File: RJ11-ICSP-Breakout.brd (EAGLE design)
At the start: 30.5 x 23 mm, 3 parts, among them J5 ICSP

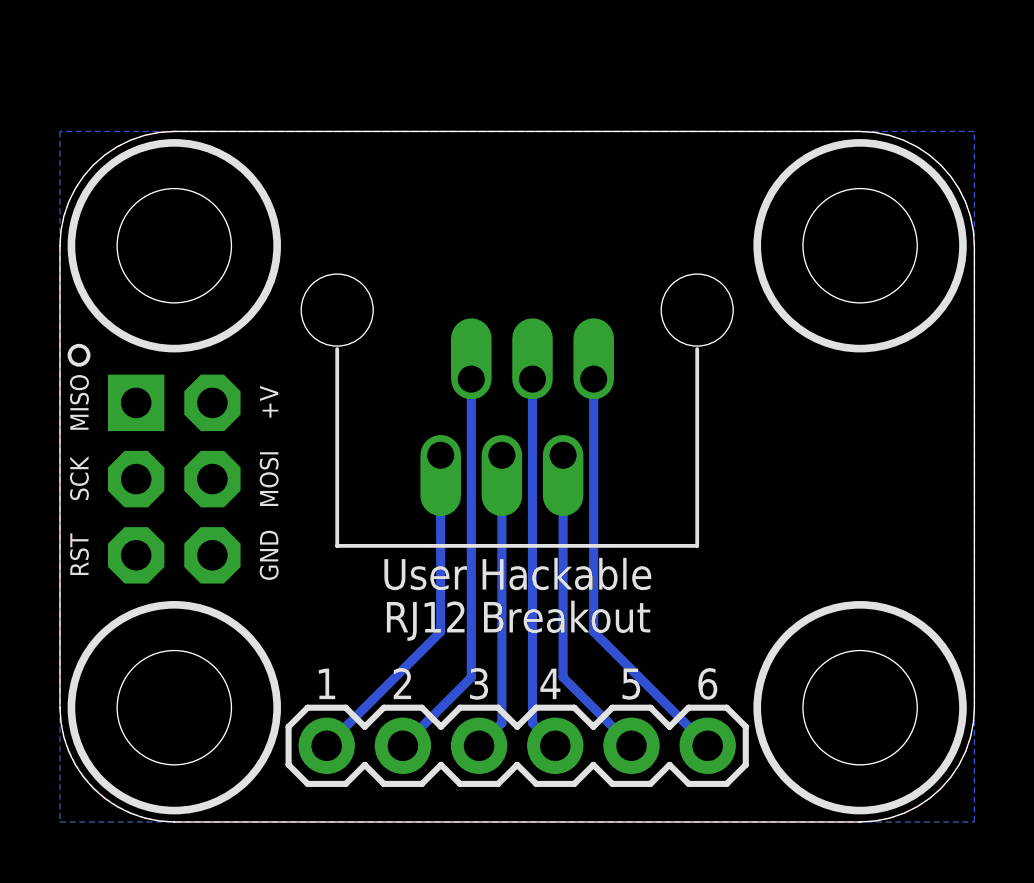
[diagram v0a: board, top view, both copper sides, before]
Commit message: updating ICSP breakout
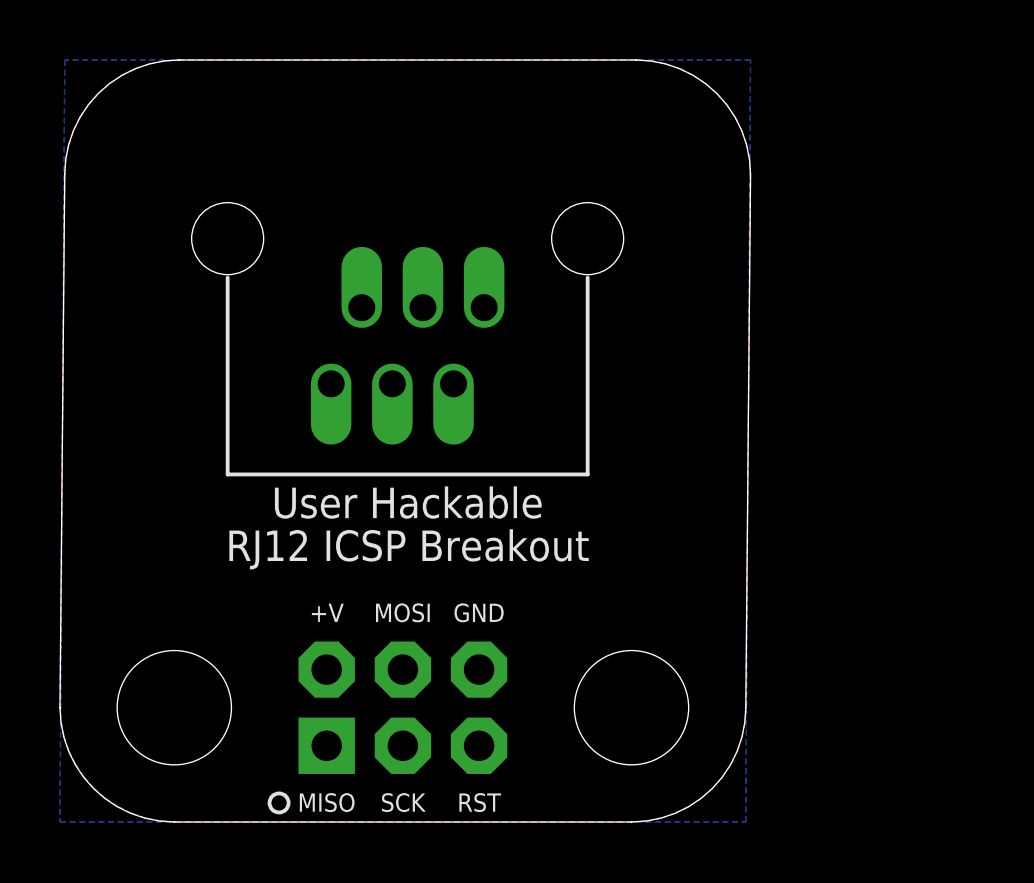
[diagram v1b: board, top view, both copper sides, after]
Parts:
- removed JP1: (no value), SparkFun-Connectors:1X06
- moved J5 10.8 mm to (11.4, 3.81), turned to 0 degrees
- moved U$7 4.36 mm to (11.6, 17.1)
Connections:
- net 4: no longer JP1.4
- net 5: no longer JP1.5
- net 5V: no longer JP1.3
- net 6: no longer JP1.6
- net GND: no longer JP1.2
- net RST: no longer JP1.1
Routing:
- net 6: track 13.8 -> 0.00 mm
- net GND: track 13.2 -> 0.00 mm
- net 4: track 12.5 -> 0.00 mm
- net RST: track 11.3 -> 0.00 mm
- net 5: track 10.6 -> 0.00 mm
- net 5V: track 10.00 -> 0.00 mm
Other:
- board size 30.5 x 23 mm -> 23 x 25.4 mm
- board text added: "RJ12 ICSP Breakout"
- board text removed: "1"
- board text removed: "2"
- board text removed: "3"
- board text removed: "4"
- board text removed: "5"
- board text removed: "6"
- board text removed: "RJ12 Breakout"
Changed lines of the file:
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@@
 <board>
 <plain>
-<wire x1="3.81" y1="0" x2="26.67" y2="0" width="0" layer="20"/>
-<wire x1="26.67" y1="0" x2="30.48" y2="3.81" width="0" layer="20" curve="90"/>
-<wire x1="30.48" y1="3.81" x2="30.48" y2="19.19554375" width="0" layer="20"/>
-<wire x1="30.48" y1="19.19554375" x2="26.65679375" y2="23.01875" width="0" layer="20" curve="90"/>
-<wire x1="26.65679375" y1="23.01875" x2="3.81" y2="23.01875" width="0" layer="20"/>
-<wire x1="3.81" y1="23.01875" x2="0" y2="19.20875" width="0" layer="20" curve="90"/>
-<wire x1="0" y1="19.20875" x2="0" y2="3.81" width="0" layer="20"/>
+<wire x1="3.81" y1="0" x2="19.05" y2="0" width="0" layer="20"/>
+<wire x1="19.05" y1="0" x2="22.86" y2="3.81" width="0" layer="20" curve="90"/>
+<wire x1="22.86" y1="3.81" x2="23.01875" y2="21.57679375" width="0" layer="20"/>
+<wire x1="23.01875" y1="21.57679375" x2="19.19554375" y2="25.4" width="0" layer="20" curve="90"/>
+<wire x1="19.19554375" y1="25.4" x2="3.96875" y2="25.4" width="0" layer="20"/>
+<wire x1="3.96875" y1="25.4" x2="0.15875" y2="21.59" width="0" layer="20" curve="90"/>
+<wire x1="0.15875" y1="21.59" x2="0" y2="3.81" width="0" layer="20"/>
 <wire x1="0" y1="3.81" x2="3.81" y2="0" width="0" layer="20" curve="90"/>
-<hole x="3.81" y="19.20875" drill="3.81"/>
 <hole x="3.81" y="3.81" drill="3.81"/>
-<circle x="3.81" y="3.81" radius="3.429" width="0.254" layer="21"/>
-<circle x="3.81" y="19.20875" radius="3.429" width="0.254" layer="21"/>
-<hole x="26.67" y="19.20875" drill="3.81"/>
-<circle x="26.67" y="19.20875" radius="3.429" width="0.254" layer="21"/>
-<hole x="26.67" y="3.81" drill="3.81"/>
-<circle x="26.67" y="3.81" radius="3.429" width="0.254" layer="21"/>
-<text x="15.24" y="8.255" size="1.016" layer="21" rot="R180" align="center">User Hackable</text>
-<text x="15.24" y="6.82625" size="1.016" layer="21" align="center">RJ12 Breakout</text>
-<text x="8.89" y="4.60375" size="1.016" layer="21" align="center">1</text>
-<text x="11.43" y="4.60375" size="1.016" layer="21" align="center">2</text>
-<text x="13.97" y="4.60375" size="1.016" layer="21" align="center">3</text>
-<text x="16.35125" y="4.60375" size="1.016" layer="21" align="center">4</text>
-<text x="19.05" y="4.60375" size="1.016" layer="21" align="center">5</text>
-<text x="21.59" y="4.60375" size="1.016" layer="21" align="center">6</text>
+<hole x="19.05" y="3.81" drill="3.81"/>
+<text x="11.58875" y="10.63625" size="1.016" layer="21" rot="R180" align="center">User Hackable</text>
+<text x="11.58875" y="9.2075" size="1.016" layer="21" align="center">RJ12 ICSP Breakout</text>
 </plain>
 <attributes>
@@
 </autorouter>
 <elements>
-<element name="J5" library="barbary_enterprises" package="2X3-NS" value="ICSP" x="3.81" y="11.43" rot="R270"/>
-<element name="U$7" library="barbary_enterprises" package="RJ12" value="RJ12" x="15.24" y="14.76375" rot="R180"/>
-<element name="JP1" library="SparkFun-Connectors" package="1X06" value="" x="8.89" y="2.54" smashed="yes">
-<attribute name="PROD_ID" value="CONN-08437" x="8.89" y="2.54" size="0.8128" layer="27" display="off"/>
-<attribute name="VALUE" x="7.62" y="-0.635" size="1.27" layer="27"/>
-</element>
+<element name="J5" library="barbary_enterprises" package="2X3-NS" value="ICSP" x="11.43" y="3.81"/>
+<element name="U$7" library="barbary_enterprises" package="RJ12" value="RJ12" x="11.58875" y="17.145" rot="R180"/>
 </elements>
 <signals>
@@
 <contactref element="J5" pad="6"/>
 <polygon width="0.4064" layer="1" isolate="0.3048">
-<vertex x="26.65679375" y="23.01875"/>
-<vertex x="3.82320625" y="23.01875" curve="90"/>
-<vertex x="0" y="19.19554375"/>
+<vertex x="19.19554375" y="25.4"/>
+<vertex x="3.98195625" y="25.4" curve="90"/>
+<vertex x="0.15875" y="21.57679375"/>
 <vertex x="0" y="3.862553125" curve="90"/>
 <vertex x="3.862553125" y="0"/>
-<vertex x="26.67" y="0" curve="90"/>
-<vertex x="30.48" y="3.81"/>
-<vertex x="30.48" y="19.19554375" curve="90"/>
+<vertex x="19.05" y="0" curve="90"/>
+<vertex x="22.86" y="3.81"/>
+<vertex x="23.01875" y="21.57679375" curve="90"/>
 </polygon>
 <polygon width="0.3048" layer="16" isolate="0.3048">
 <vertex x="0" y="0"/>
-<vertex x="30.48" y="0"/>
-<vertex x="30.48" y="23.01875"/>
-<vertex x="0" y="23.01875"/>
+<vertex x="22.86" y="0"/>
+<vertex x="23.01875" y="25.4"/>
+<vertex x="0.15875" y="25.4"/>
 </polygon>
 <contactref element="U$7" pad="2"/>
-<contactref element="JP1" pad="2"/>
-<wire x1="13.71" y1="14.76375" x2="13.71" y2="4.82" width="0.3048" layer="16"/>
-<wire x1="13.71" y1="4.82" x2="11.43" y2="2.54" width="0.3048" layer="16"/>
-<wire x1="11.43" y1="2.54" x2="5.08" y2="8.89" width="0" layer="19" extent="1-1"/>
+<wire x1="13.97" y1="5.08" x2="10.05875" y2="17.145" width="0" layer="19" extent="1-1"/>
 </signal>
 <signal name="5V">
 <contactref element="J5" pad="2"/>
 <contactref element="U$7" pad="3"/>
-<contactref element="JP1" pad="3"/>
-<wire x1="5.08" y1="13.97" x2="14.73" y2="12.22375" width="0" layer="19" extent="1-1"/>
-<wire x1="14.73" y1="12.22375" x2="14.73" y2="3.3" width="0.3048" layer="16"/>
-<wire x1="14.73" y1="3.3" x2="13.97" y2="2.54" width="0.3048" layer="16"/>
+<wire x1="8.89" y1="5.08" x2="11.07875" y2="14.605" width="0" layer="19" extent="1-1"/>
 </signal>
 <signal name="4">
 <contactref element="J5" pad="3"/>
 <contactref element="U$7" pad="4"/>
-<contactref element="JP1" pad="4"/>
-<wire x1="2.54" y1="11.43" x2="15.75" y2="14.76375" width="0" layer="19" extent="1-1"/>
-<wire x1="15.75" y1="14.76375" x2="15.75" y2="3.3" width="0.3048" layer="16"/>
-<wire x1="15.75" y1="3.3" x2="16.51" y2="2.54" width="0.3048" layer="16"/>
+<wire x1="11.43" y1="2.54" x2="12.09875" y2="17.145" width="0" layer="19" extent="1-1"/>
 </signal>
 <signal name="5">
 <contactref element="J5" pad="1"/>
 <contactref element="U$7" pad="5"/>
-<contactref element="JP1" pad="5"/>
-<wire x1="2.54" y1="13.97" x2="16.77" y2="12.22375" width="0" layer="19" extent="1-1"/>
-<wire x1="16.77" y1="12.22375" x2="16.77" y2="4.82" width="0.3048" layer="16"/>
-<wire x1="16.77" y1="4.82" x2="19.05" y2="2.54" width="0.3048" layer="16"/>
+<wire x1="8.89" y1="2.54" x2="13.11875" y2="14.605" width="0" layer="19" extent="1-1"/>
 </signal>
 <signal name="6">
 <contactref element="J5" pad="4"/>
 <contactref element="U$7" pad="6"/>
-<contactref element="JP1" pad="6"/>
-<wire x1="5.08" y1="11.43" x2="17.79" y2="14.76375" width="0" layer="19" extent="1-1"/>
-<wire x1="17.79" y1="14.76375" x2="17.79" y2="6.34" width="0.3048" layer="16"/>
-<wire x1="17.79" y1="6.34" x2="21.59" y2="2.54" width="0.3048" layer="16"/>
+<wire x1="11.43" y1="5.08" x2="14.13875" y2="17.145" width="0" layer="19" extent="1-1"/>
 </signal>
 <signal name="RST">
 <contactref element="J5" pad="5"/>
 <contactref element="U$7" pad="1"/>
-<contactref element="JP1" pad="1"/>
-<wire x1="2.54" y1="8.89" x2="8.89" y2="2.54" width="0" layer="19" extent="1-1"/>
-<wire x1="12.69" y1="12.22375" x2="12.69" y2="6.34" width="0.3048" layer="16"/>
-<wire x1="12.69" y1="6.34" x2="8.89" y2="2.54" width="0.3048" layer="16"/>
+<wire x1="13.97" y1="2.54" x2="9.03875" y2="14.605" width="0" layer="19" extent="1-1"/>
 </signal>
 </signals>

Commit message: update ICSP breakout
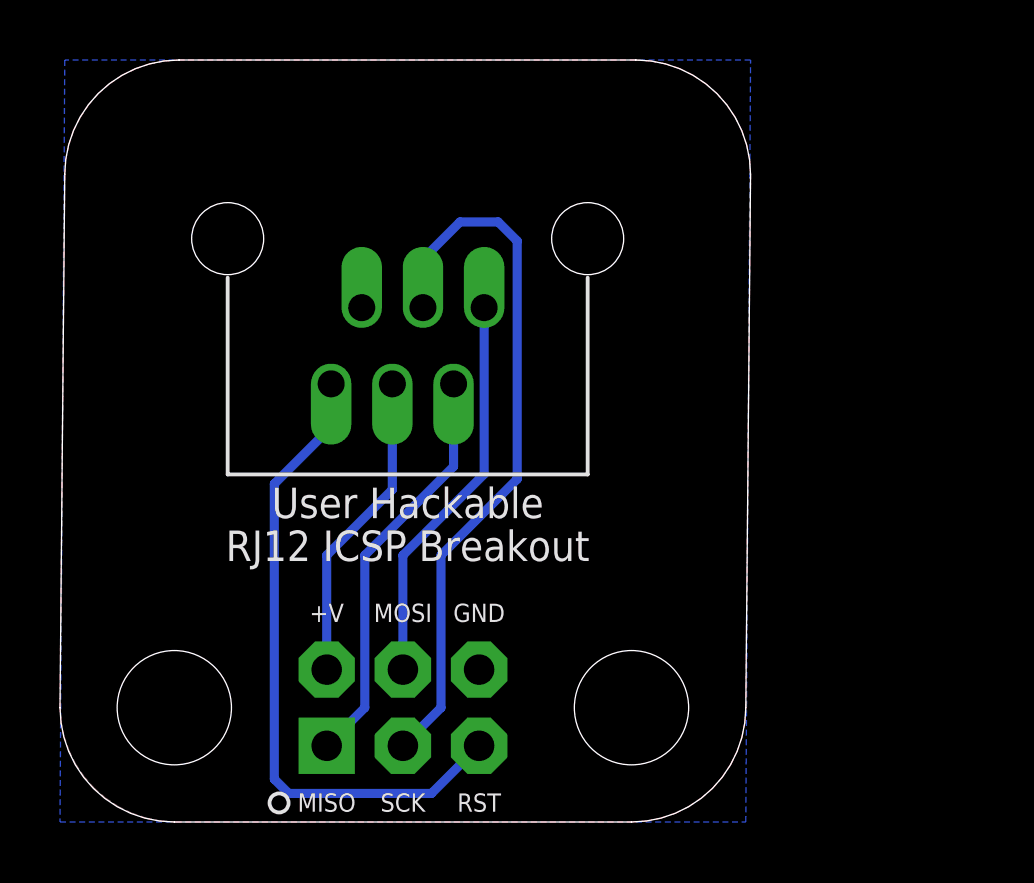
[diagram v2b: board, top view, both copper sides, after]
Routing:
- net 4: track 0.00 -> 24.0 mm
- net RST: track 0.00 -> 21.7 mm
- net 5: track 0.00 -> 13.8 mm
- net 6: track 0.00 -> 13.2 mm
- net 5V: track 0.00 -> 10.4 mm
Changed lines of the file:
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@@
 </polygon>
 <contactref element="U$7" pad="2"/>
-<wire x1="13.97" y1="5.08" x2="10.05875" y2="17.145" width="0" layer="19" extent="1-1"/>
 </signal>
 <signal name="5V">
 <contactref element="J5" pad="2"/>
 <contactref element="U$7" pad="3"/>
-<wire x1="8.89" y1="5.08" x2="11.07875" y2="14.605" width="0" layer="19" extent="1-1"/>
+<wire x1="8.89" y1="5.08" x2="8.89" y2="8.89" width="0.3048" layer="16"/>
+<wire x1="8.89" y1="8.89" x2="11.07875" y2="11.07875" width="0.3048" layer="16"/>
+<wire x1="11.07875" y1="11.07875" x2="11.07875" y2="14.605" width="0.3048" layer="16"/>
 </signal>
 <signal name="4">
 <contactref element="J5" pad="3"/>
 <contactref element="U$7" pad="4"/>
-<wire x1="11.43" y1="2.54" x2="12.09875" y2="17.145" width="0" layer="19" extent="1-1"/>
+<wire x1="11.43" y1="2.54" x2="12.7" y2="3.81" width="0.3048" layer="16"/>
+<wire x1="12.7" y1="3.81" x2="12.7" y2="8.89" width="0.3048" layer="16"/>
+<wire x1="12.7" y1="8.89" x2="15.24" y2="11.43" width="0.3048" layer="16"/>
+<wire x1="15.24" y1="11.43" x2="15.24" y2="19.3675" width="0.3048" layer="16"/>
+<wire x1="15.24" y1="19.3675" x2="14.605" y2="20.0025" width="0.3048" layer="16"/>
+<wire x1="14.605" y1="20.0025" x2="13.335" y2="20.0025" width="0.3048" layer="16"/>
+<wire x1="13.335" y1="20.0025" x2="12.065" y2="18.7325" width="0.3048" layer="16"/>
+<wire x1="12.065" y1="18.7325" x2="12.065" y2="17.17875" width="0.3048" layer="16"/>
+<wire x1="12.065" y1="17.17875" x2="12.09875" y2="17.145" width="0.3048" layer="16"/>
 </signal>
 <signal name="5">
 <contactref element="J5" pad="1"/>
 <contactref element="U$7" pad="5"/>
-<wire x1="8.89" y1="2.54" x2="13.11875" y2="14.605" width="0" layer="19" extent="1-1"/>
+<wire x1="8.89" y1="2.54" x2="10.16" y2="3.81" width="0.3048" layer="16"/>
+<wire x1="10.16" y1="3.81" x2="10.16" y2="8.89" width="0.3048" layer="16"/>
+<wire x1="10.16" y1="8.89" x2="13.11875" y2="11.84875" width="0.3048" layer="16"/>
+<wire x1="13.11875" y1="11.84875" x2="13.11875" y2="14.605" width="0.3048" layer="16"/>
 </signal>
 <signal name="6">
 <contactref element="J5" pad="4"/>
 <contactref element="U$7" pad="6"/>
-<wire x1="11.43" y1="5.08" x2="14.13875" y2="17.145" width="0" layer="19" extent="1-1"/>
+<wire x1="11.43" y1="5.08" x2="11.43" y2="8.89" width="0.3048" layer="16"/>
+<wire x1="11.43" y1="8.89" x2="14.13875" y2="11.59875" width="0.3048" layer="16"/>
+<wire x1="14.13875" y1="11.59875" x2="14.13875" y2="17.145" width="0.3048" layer="16"/>
 </signal>
 <signal name="RST">
 <contactref element="J5" pad="5"/>
 <contactref element="U$7" pad="1"/>
-<wire x1="13.97" y1="2.54" x2="9.03875" y2="14.605" width="0" layer="19" extent="1-1"/>
+<wire x1="13.97" y1="2.54" x2="12.3825" y2="0.9525" width="0.3048" layer="16"/>
+<wire x1="12.3825" y1="0.9525" x2="7.62" y2="0.9525" width="0.3048" layer="16"/>
+<wire x1="7.62" y1="0.9525" x2="7.14375" y2="1.42875" width="0.3048" layer="16"/>
+<wire x1="7.14375" y1="1.42875" x2="7.14375" y2="11.27125" width="0.3048" layer="16"/>
+<wire x1="7.14375" y1="11.27125" x2="9.04875" y2="13.17625" width="0.3048" layer="16"/>
+<wire x1="9.04875" y1="13.17625" x2="9.04875" y2="14.595" width="0.3048" layer="16"/>
+<wire x1="9.04875" y1="14.595" x2="9.03875" y2="14.605" width="0.3048" layer="16"/>
 </signal>
 </signals>
